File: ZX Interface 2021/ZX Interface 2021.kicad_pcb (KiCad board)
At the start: 2 copper layers, 87.6 x 99.9 mm, 58 parts, among them J1 JOYSTICK 2, J2 JOYSTICK 1, J3 BA14_HI, J4 Extended Cartridge Port, J5 JOYSTICK_EN, M1 Mounting, M2 Mounting, M3 Mounting, M4 Mounting, M5 Mounting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

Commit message: Gerber export
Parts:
- moved Q1 0.38 mm to (187.3, 129.8)
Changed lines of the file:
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@@
     (thickness 1.6)
     (drawings 75)
-    (tracks 1322)
+    (tracks 1325)
     (zones 0)
     (modules 58)
@@
   )
   (module Package_TO_SOT_THT:TO-92_Inline_Wide (layer F.Cu)
-    (at 187.325 130.175 90)
+    (at 187.325 129.794 90)
     (descr "TO-92 leads in-line, wide, drill 0.75mm (see NXP sot054_po.pdf)")
     (tags "to-92 sc-43 sc-43a sot54 PA33 transistor")
-    (fp_text reference Q1 (at 2.54 -3.56 90) (layer F.SilkS)
-      (effects (font (size 1 1) (thickness 0.15)))
+    (fp_text reference Q1 (at 5.715 -1.905 180) (layer F.SilkS)
+      (effects (font (size 0.8 0.8) (thickness 0.1)))
     )
-    (fp_text value 2N3904 (at 2.54 2.79 90) (layer F.Fab)
-      (effects (font (size 1 1) (thickness 0.15)))
+    (fp_text value 2N3904 (at -1.778 0 180) (layer F.SilkS)
+      (effects (font (size 0.8 0.8) (thickness 0.1)))
     )
     (fp_line (start 6.09 2.01) (end -1.01 2.01) (layer F.CrtYd) (width 0.05))
@@
   (segment (start 162.56 116.205) (end 163.595031 117.240031) (width 0.381) (layer B.Cu) (net 2))
   (segment (start 163.595031 117.240031) (end 184.385001 117.240031) (width 0.381) (layer B.Cu) (net 2))
-  (segment (start 188.595 123.825) (end 187.325 125.095) (width 0.381) (layer F.Cu) (net 2) (status 20))
   (segment (start 188.595 118.11) (end 188.595 123.825) (width 0.381) (layer F.Cu) (net 2))
   (segment (start 108.331 130.175) (end 108.458 130.302) (width 0.381) (layer F.Cu) (net 2))
@@
   (segment (start 104.14 96.52) (end 114.3 86.36) (width 0.381) (layer F.Cu) (net 2))
   (segment (start 104.14 106.045) (end 104.14 96.52) (width 0.381) (layer F.Cu) (net 2))
+  (segment (start 187.325 124.714) (end 187.96 124.714) (width 0.381) (layer F.Cu) (net 2))
+  (segment (start 188.595 124.079) (end 188.595 123.825) (width 0.381) (layer F.Cu) (net 2))
+  (segment (start 187.96 124.714) (end 188.595 124.079) (width 0.381) (layer F.Cu) (net 2))
   (segment (start 124.46 52.07) (end 124.46 52.451) (width 0.25) (layer F.Cu) (net 3) (status 30))
   (segment (start 120.65 61.976) (end 120.65 62.23) (width 0.25) (layer F.Cu) (net 3) (status 30))
@@
   (segment (start 173.355 132.628996) (end 173.355 132.08) (width 0.25) (layer B.Cu) (net 60))
   (segment (start 175.26 130.175) (end 174.625 130.81) (width 0.25) (layer F.Cu) (net 60))
-  (segment (start 187.325 130.175) (end 175.26 130.175) (width 0.25) (layer F.Cu) (net 60) (status 10))
+  (segment (start 175.641 129.794) (end 175.26 130.175) (width 0.25) (layer F.Cu) (net 60))
+  (segment (start 187.325 129.794) (end 175.641 129.794) (width 0.25) (layer F.Cu) (net 60))
   (segment (start 152.4 136.525) (end 152.4 136.3695) (width 0.25) (layer F.Cu) (net 61))
   (segment (start 174.625 133.35) (end 174.625 132.207) (width 0.25) (layer F.Cu) (net 61) (status 30))
@@
   (segment (start 174.625 77.47) (end 174.625 82.55) (width 0.25) (layer F.Cu) (net 75))
   (segment (start 174.625 82.55) (end 172.72 84.455) (width 0.25) (layer F.Cu) (net 75) (status 20))
-  (segment (start 187.325 127.635) (end 186.055 127.635) (width 0.25) (layer F.Cu) (net 76) (status 10))
-  (segment (start 186.055 127.635) (end 185.42 127) (width 0.25) (layer F.Cu) (net 76))
-  (segment (start 185.42 127) (end 185.42 122.555) (width 0.25) (layer F.Cu) (net 76))
   (segment (start 186.055 121.92) (end 186.69 121.92) (width 0.25) (layer F.Cu) (net 76) (status 30))
   (segment (start 185.42 122.555) (end 186.055 121.92) (width 0.25) (layer F.Cu) (net 76) (status 20))
+  (segment (start 186.182 127.254) (end 185.42 126.492) (width 0.25) (layer F.Cu) (net 76))
+  (segment (start 187.325 127.254) (end 186.182 127.254) (width 0.25) (layer F.Cu) (net 76))
+  (segment (start 185.42 126.492) (end 185.42 122.555) (width 0.25) (layer F.Cu) (net 76))
   (segment (start 175.895 123.19) (end 175.895 128.016) (width 0.25) (layer F.Cu) (net 77))
   (segment (start 175.895 128.016) (end 173.355 130.556) (width 0.25) (layer F.Cu) (net 77))

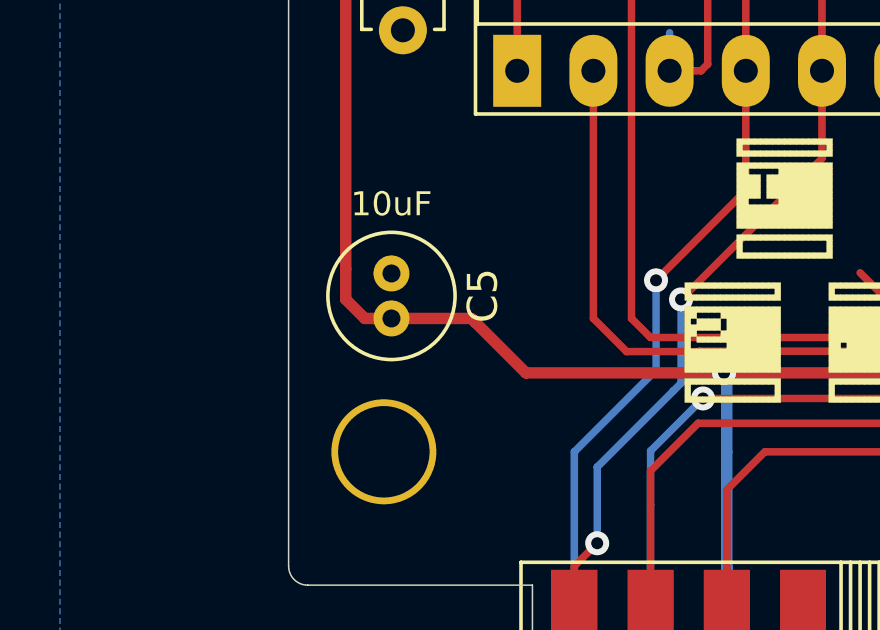
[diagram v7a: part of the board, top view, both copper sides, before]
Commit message: Marked positive C5 pin
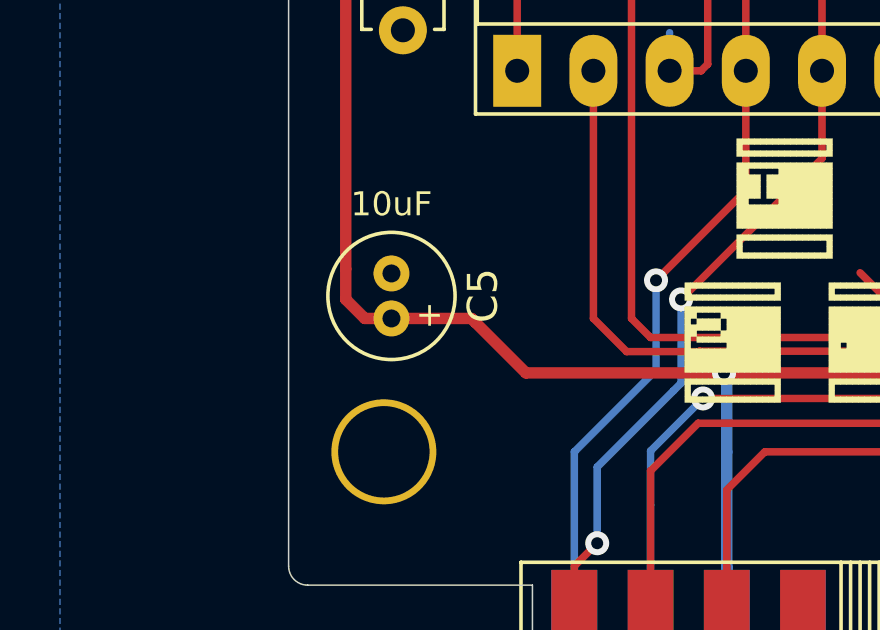
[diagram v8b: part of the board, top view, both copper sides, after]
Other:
- board text added: "+"
